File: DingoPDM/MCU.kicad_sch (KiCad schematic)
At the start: 29 parts, among them J4 TC, SW1 BOOT, U3 PCA82C250, U4 STM32F446RETx, Y1 8mHz

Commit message: Status and Error LED part num switched
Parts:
- D3: value GRN -> RED; Digi-Key_PN 475-1410-1-ND -> 475-1278-1-ND; LCSC C2899888 -> C2899997
- D5: value RED -> GRN; Digi-Key_PN 475-1278-1-ND -> 475-1410-1-ND; LCSC C2899997 -> C2899888
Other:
- note added: "Error"
- note added: "Status"
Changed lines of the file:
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@@
     (effects (font (size 1.27 1.27) (thickness 0.254) bold) (justify right bottom))
+  )
+  (text "Error" (at 27.94 66.675 0)
+    (effects (font (size 1.27 1.27)) (justify left bottom))
   )
   (text "CAN Transceiver" (at 158.115 143.51 0)
@@
   (text "VDDA" (at 243.84 22.86 0)
     (effects (font (size 1.27 1.27)) (justify right bottom))
+  )
+  (text "Status" (at 43.815 74.295 0)
+    (effects (font (size 1.27 1.27)) (justify left bottom))
   )
   (label "CAN_TX" (at 64.135 151.13 90) (fields_autoplaced)
@@
       (effects (font (size 1.27 1.27)))
     )
-    (property "Value" "GRN" (at 20.955 66.04 90)
+    (property "Value" "RED" (at 20.955 66.04 90)
       (effects (font (size 1.27 1.27)))
     )
@@
       (effects (font (size 1.27 1.27)) hide)
     )
-    (property "Digi-Key_PN" "475-1410-1-ND" (at 25.4 66.04 0)
-      (effects (font (size 1.27 1.27)) hide)
-    )
-    (property "LCSC" "C2899888" (at 25.4 66.04 0)
+    (property "Digi-Key_PN" "475-1278-1-ND" (at 25.4 66.04 0)
+      (effects (font (size 1.27 1.27)) hide)
+    )
+    (property "LCSC" "C2899997" (at 25.4 66.04 0)
       (effects (font (size 1.27 1.27)) hide)
     )
@@
       (effects (font (size 1.27 1.27)))
     )
-    (property "Value" "RED" (at 40.005 72.39 90)
+    (property "Value" "GRN" (at 40.005 72.39 90)
       (effects (font (size 1.27 1.27)))
     )
@@
       (effects (font (size 1.27 1.27)) hide)
     )
-    (property "Digi-Key_PN" "475-1278-1-ND" (at 36.195 73.025 0)
-      (effects (font (size 1.27 1.27)) hide)
-    )
-    (property "LCSC" "C2899997" (at 36.195 73.025 0)
-      (effects (font (size 1.27 1.27)) hide)
-    )
+    (property "Digi-Key_PN" "475-1410-1-ND" (at 36.195 73.025 0)
+      (effects (font (size 1.27 1.27)) hide)
+    )
+    (property "LCSC" "C2899888" (at 36.195 73.025 0)
+      (effects (font (size 1.27 1.27)) hide)
+    )

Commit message: Fixed USB, power LED and CAN standby
And increased screw hole size
#9, #11, #12, #13
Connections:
- net GND: no longer U3.8 (Rs)
- net CAN_STANDBY: now reaches U4.53 (PC12)
- net CAN_STANDBY: now also U3.8 (Rs)
- no-connect marks 9 -> 8
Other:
- moved on the sheet: C9
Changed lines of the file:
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@@
   (title_block
     (title "Dingo_PDM")
-    (date "2023-09-11")
-    (rev "v7.2")
+    (date "2024-05-26")
+    (rev "v7.3")
     (comment 3 "github.com/corygrant")
     (comment 4 "Cory Grant")
@@
   (no_connect (at 127 111.125))
   (no_connect (at 127 57.785))
-  (no_connect (at 91.44 90.805))
   (no_connect (at 127 75.565))
   (no_connect (at 91.44 95.885))
@@
     (stroke (width 0) (type default))
   )
-  (wire (pts (xy 83.185 175.26) (xy 83.185 177.8))
+  (wire (pts (xy 83.185 175.26) (xy 83.185 181.61))
     (stroke (width 0) (type default))
   )
@@
     (stroke (width 0) (type default))
   )
+  (wire (pts (xy 83.185 181.61) (xy 76.835 181.61))
+    (stroke (width 0) (type default))
+  )
   (wire (pts (xy 54.61 50.165) (xy 54.61 52.705))
     (stroke (width 0) (type default))
@@
   )
   (wire (pts (xy 111.76 23.495) (xy 111.76 32.385))
+    (stroke (width 0) (type default))
+  )
+  (wire (pts (xy 83.185 90.805) (xy 91.44 90.805))
     (stroke (width 0) (type default))
   )
@@
   (label "SWO" (at 138.43 88.265 0) (fields_autoplaced)
     (effects (font (size 1.27 1.27)) (justify left bottom))
+  )
+  (label "CAN_STANDBY" (at 76.835 181.61 180) (fields_autoplaced)
+    (effects (font (size 1.27 1.27)) (justify right bottom))
+  )
+  (label "CAN_STANDBY" (at 83.185 90.805 180) (fields_autoplaced)
+    (effects (font (size 1.27 1.27)) (justify right bottom))
   )
   (label "CAN_RX" (at 79.375 167.64 180) (fields_autoplaced)
@@
     )
   )
-  (symbol (lib_id "power:GND") (at 83.185 177.8 0) (unit 1)
-    (in_bom yes) (on_board yes) (dnp no)
-    (property "Reference" "#PWR029" (at 83.185 184.15 0)
-      (effects (font (size 1.27 1.27)) hide)
-    )
-    (property "Value" "GND" (at 83.312 182.1942 0)
-      (effects (font (size 1.27 1.27)))
-    )
-    (property "Footprint" "" (at 83.185 177.8 0)
-      (effects (font (size 1.27 1.27)) hide)
-    )
-    (property "Datasheet" "" (at 83.185 177.8 0)
-      (effects (font (size 1.27 1.27)) hide)
-    )
-    (pin "1")
-    (instances
-      (project "DingoPDM"
-        (path "/8948e307-9174-4227-9c28-3ff885e6e83d/00000000-0000-0000-0000-00005f4db108"
-          (reference "#PWR029") (unit 1)
-        )
-      )
-    )
-  )
   (symbol (lib_id "power:+3V3") (at 76.835 175.26 0) (unit 1)
     (in_bom yes) (on_board yes) (dnp no)
@@
     )
   )
-  (symbol (lib_id "Device:C_Small") (at 66.675 185.42 0) (unit 1)
-    (in_bom yes) (on_board yes) (dnp no)
-    (property "Reference" "C9" (at 73.025 184.15 0)
-      (effects (font (size 1.27 1.27)))
-    )
-    (property "Value" "100nF" (at 73.025 186.69 0)
-      (effects (font (size 1.27 1.27)))
-    )
-    (property "Footprint" "Capacitor_SMD:C_0805_2012Metric" (at 66.675 185.42 0)
-      (effects (font (size 1.27 1.27)) hide)
-    )
-    (property "Datasheet" "" (at 66.675 185.42 0)
-      (effects (font (size 1.27 1.27)) hide)
-    )
-    (property "Digi-Key_PN" "478-1395-1-ND" (at 66.675 185.42 0)
-      (effects (font (size 1.27 1.27)) hide)
-    )
-    (property "LCSC" "C49678" (at 66.675 185.42 0)
+  (symbol (lib_id "Device:C_Small") (at 59.055 193.04 0) (unit 1)
+    (in_bom yes) (on_board yes) (dnp no)
+    (property "Reference" "C9" (at 65.405 191.77 0)
+      (effects (font (size 1.27 1.27)))
+    )
+    (property "Value" "100nF" (at 65.405 194.31 0)
+      (effects (font (size 1.27 1.27)))
+    )
+    (property "Footprint" "Capacitor_SMD:C_0805_2012Metric" (at 59.055 193.04 0)
+      (effects (font (size 1.27 1.27)) hide)
+    )
+    (property "Datasheet" "" (at 59.055 193.04 0)
+      (effects (font (size 1.27 1.27)) hide)
+    )
+    (property "Digi-Key_PN" "478-1395-1-ND" (at 59.055 193.04 0)
+      (effects (font (size 1.27 1.27)) hide)
+    )
+    (property "LCSC" "C49678" (at 59.055 193.04 0)
       (effects (font (size 1.27 1.27)) hide)
     )
@@
     )
   )
-  (symbol (lib_id "power:+3V3") (at 66.675 182.88 0) (unit 1)
-    (in_bom yes) (on_board yes) (dnp no)
-    (property "Reference" "#PWR024" (at 66.675 186.69 0)
-      (effects (font (size 1.27 1.27)) hide)
-    )
-    (property "Value" "+3V3" (at 67.056 178.4858 0)
-      (effects (font (size 1.27 1.27)))
-    )
-    (property "Footprint" "" (at 66.675 182.88 0)
-      (effects (font (size 1.27 1.27)) hide)
-    )
-    (property "Datasheet" "" (at 66.675 182.88 0)
+  (symbol (lib_id "power:+3V3") (at 59.055 190.5 0) (unit 1)
+    (in_bom yes) (on_board yes) (dnp no)
+    (property "Reference" "#PWR024" (at 59.055 194.31 0)
+      (effects (font (size 1.27 1.27)) hide)
+    )
+    (property "Value" "+3V3" (at 59.436 186.1058 0)
+      (effects (font (size 1.27 1.27)))
+    )
+    (property "Footprint" "" (at 59.055 190.5 0)
+      (effects (font (size 1.27 1.27)) hide)
+    )
+    (property "Datasheet" "" (at 59.055 190.5 0)
       (effects (font (size 1.27 1.27)) hide)
     )
@@
     )
   )
-  (symbol (lib_id "power:GND") (at 66.675 187.96 0) (unit 1)
-    (in_bom yes) (on_board yes) (dnp no)
-    (property "Reference" "#PWR025" (at 66.675 194.31 0)
-      (effects (font (size 1.27 1.27)) hide)
-    )
-    (property "Value" "GND" (at 66.802 192.3542 0)
-      (effects (font (size 1.27 1.27)))
-    )
-    (property "Footprint" "" (at 66.675 187.96 0)
-      (effects (font (size 1.27 1.27)) hide)
-    )
-    (property "Datasheet" "" (at 66.675 187.96 0)
-      (effects (font (size 1.27 1.27)) hide)
-    )
+  (symbol (lib_id "power:GND") (at 59.055 195.58 0) (unit 1)
+    (in_bom yes) (on_board yes) (dnp no)
+    (property "Reference" "#PWR025" (at 59.055 201.93 0)
+      (effects (font (size 1.27 1.27)) hide)
+    )
+    (property "Value" "GND" (at 59.182 199.9742 0)
+      (effects (font (size 1.27 1.27)))
+    )
+    (property "Footprint" "" (at 59.055 195.58 0)
+      (effects (font (size 1.27 1.27)) hide)
+    )
+    (property "Datasheet" "" (at 59.055 195.58 0)
+      (effects (font (size 1.27 1.27)) hide)
+    )

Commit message: Updated to Kicad 8
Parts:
- renumbered D3 to D16, D5 to D17, R3 to R52, R3 to R53

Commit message: add DC-DC converter options
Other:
- title: Dingo_PDM -> dingoPDM

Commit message: move footprints to project library
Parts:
- D4: footprint digikey-footprints:SOT-23-3 -> dingoPDM:SOT-23-3
- SW1: footprint SlideSwitch:CJS-1200TB -> dingoPDM:CJS-1200TB
- Y1: footprint Crystals_Modify:Crystal_SMD_5032-2Pin_5.0x3.2mm_HandSoldering -> dingoPDM:Crystal_SMD_5032-2Pin_5.0x3.2mm_HandSoldering
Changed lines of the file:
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@@
 			)
 		)
-		(property "Footprint" "Crystals_Modify:Crystal_SMD_5032-2Pin_5.0x3.2mm_HandSoldering"
+		(property "Footprint" "dingoPDM:Crystal_SMD_5032-2Pin_5.0x3.2mm_HandSoldering"
 			(at 38.1 46.355 0)
 			(effects
@@
 			)
 		)
-		(property "Footprint" "digikey-footprints:SOT-23-3"
+		(property "Footprint" "dingoPDM:SOT-23-3"
 			(at 132.715 187.96 0)
 			(effects
@@
 			)
 		)
-		(property "Footprint" "SlideSwitch:CJS-1200TB"
+		(property "Footprint" "dingoPDM:CJS-1200TB"
 			(at 69.85 31.115 0)
 			(effects

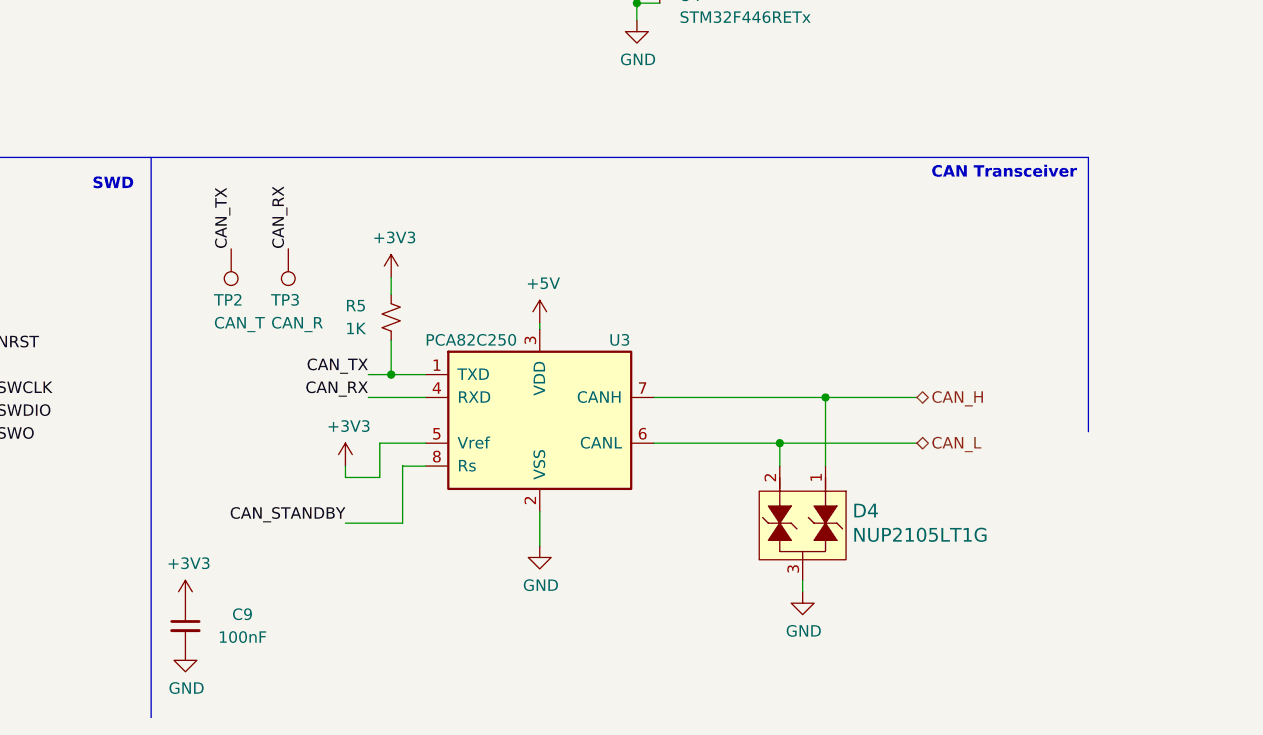
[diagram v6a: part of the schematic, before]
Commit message: make v7.6 changes, update can transceiver
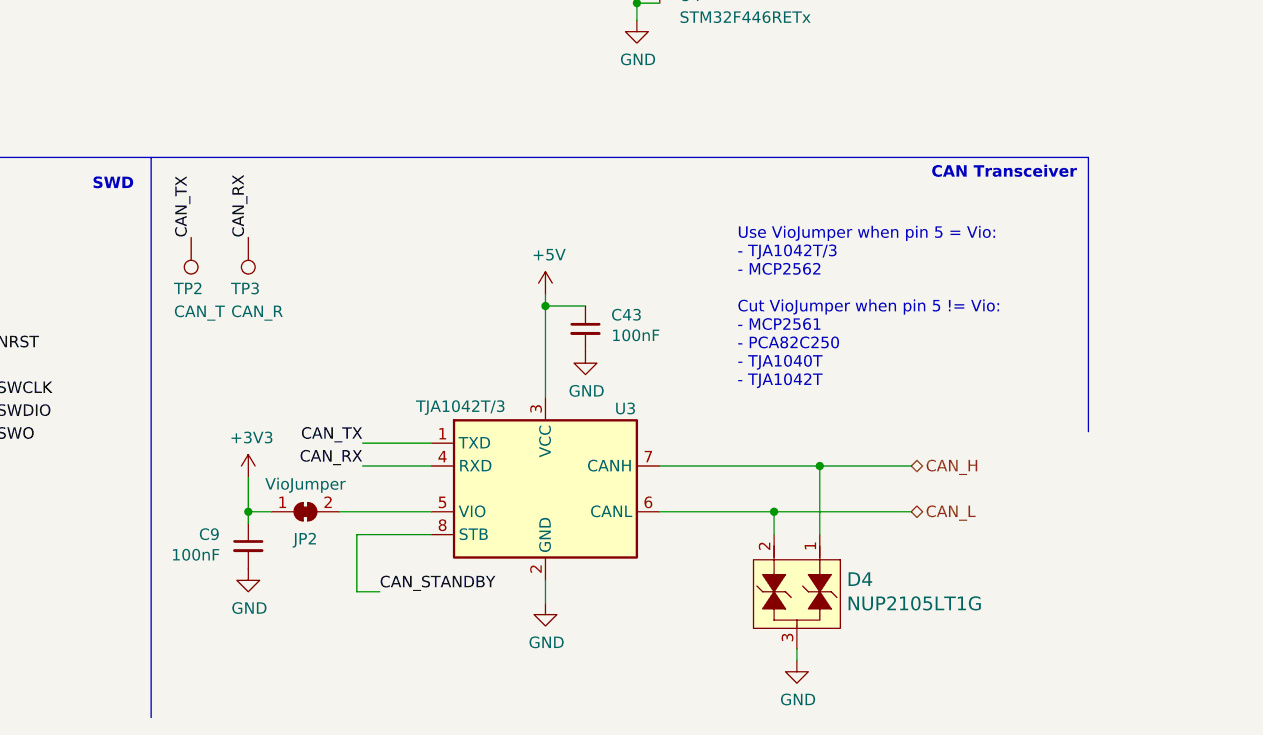
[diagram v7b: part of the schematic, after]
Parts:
- removed R5: 1K, Resistor_SMD:R_0805_2012Metric, symbol Device:R_Small_US
- added C43: 100nF, Capacitor_SMD:C_0805_2012Metric, symbol Device:C_Small
- added JP2: VioJumper, Jumper:SolderJumper-2_P1.3mm_Bridged_RoundedPad1.0x1.5mm, symbol Jumper:SolderJumper_2_Bridged
- U3: value PCA82C250 -> TJA1042T/3; symbol Interface_CAN_LIN:MCP2551-I-SN -> Interface_CAN_LIN:TJA1042T-3; Digi-Key_PN 568-10316-1-ND -> 568-12625-1-ND; LCSC C7439 -> C132227
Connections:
- net +3V3: now also JP2.1 (A); no longer U3.5 (Vref)
- net +5V: now also C43.1
- net GND: now also C43.2
- new net: JP2.2 (B), U3.5 (VIO)
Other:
- note added: "Use VioJumper when pin 5 = Vio: - TJA1042T/3 - MCP2562 Cut VioJumper when pin 5 != Vio: - MCP2561 - PCA82C250 - TJA1040T - TJA1042T"
- moved on the sheet: C9, D4, TP2, TP3, U3
